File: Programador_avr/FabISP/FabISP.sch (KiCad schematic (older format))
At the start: 14 parts, among them IC1 ATTINY44-SSU, M1 Reson., M2 PINHD-1x02-SMD-HEADER, M3 MICRO-USB_1_64, M4 PINHD-1x02-SMD-HEADER

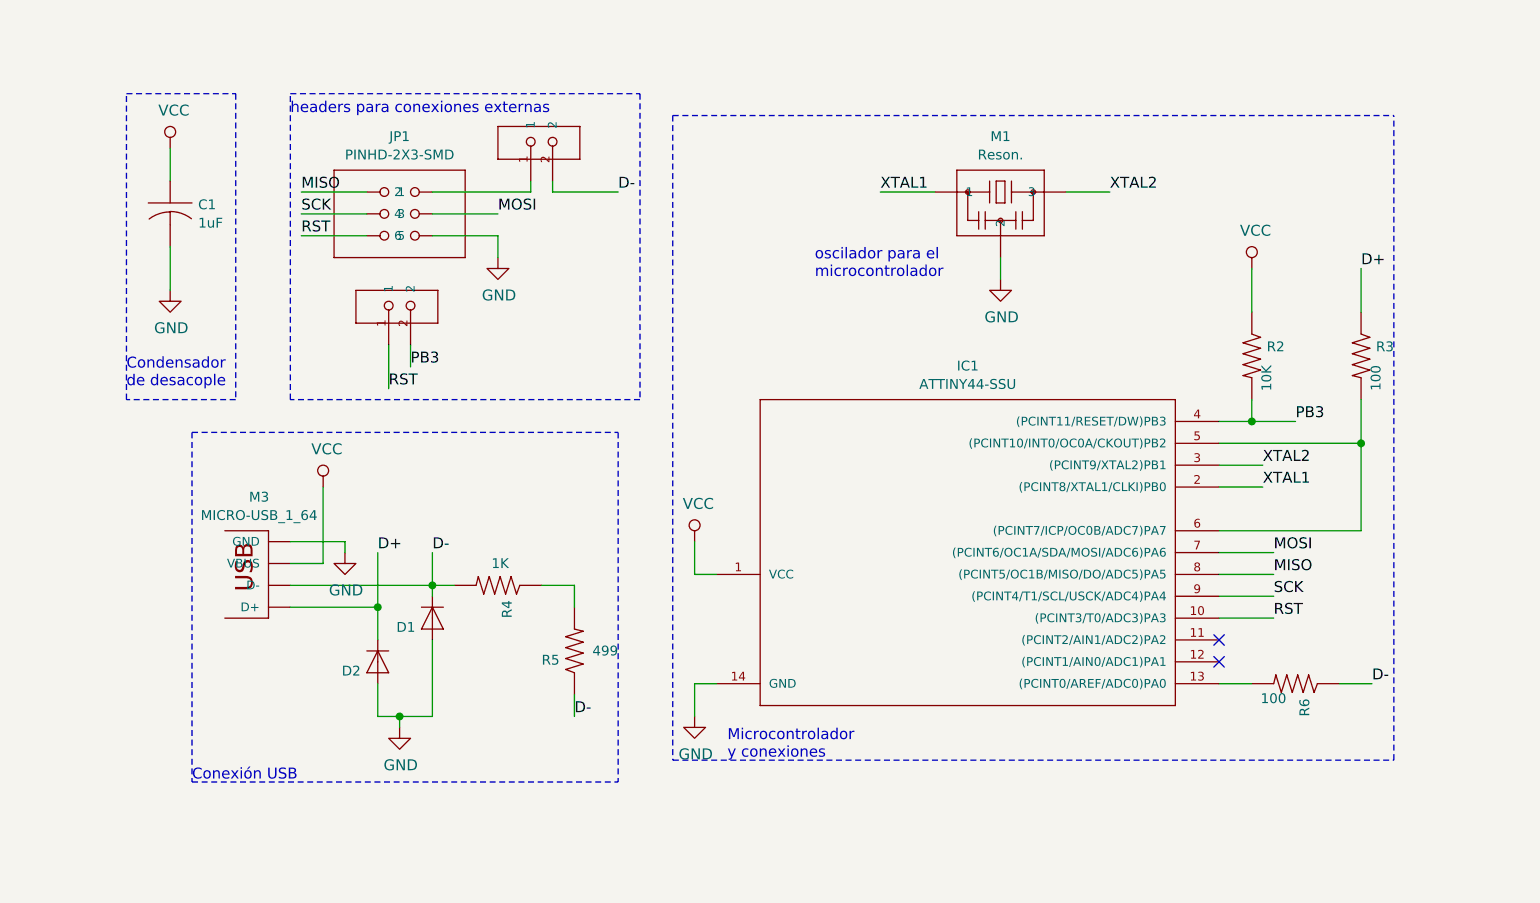
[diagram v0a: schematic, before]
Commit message: Corrección SCH Se hicieron las conexiones reemplazando etiquetas se agrego información de componentes se agregó información solicitada
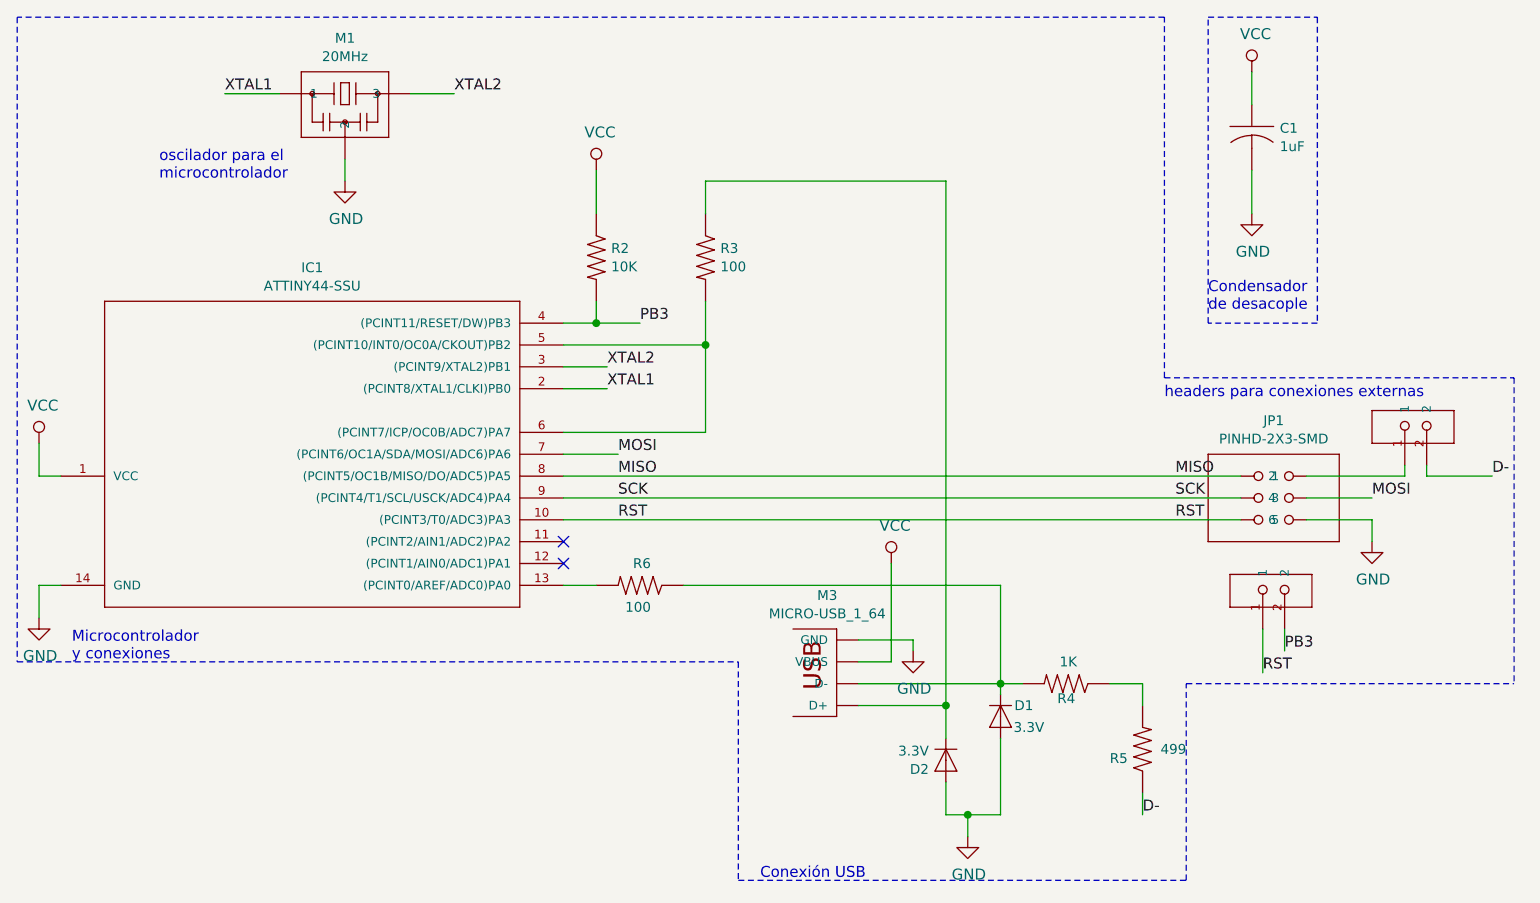
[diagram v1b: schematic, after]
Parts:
- D1, D2: value (none) -> 3.3V
- M1: value Reson. -> 20MHz
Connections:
- net D-: no longer D1.CATHODE (C), M3.D-, R4.2, R6.1
- net D+: no longer names the net of D2.CATHODE (C), M3.D+, R3.1
- new net: D1.CATHODE (C), M3.D-, R4.2, R6.1
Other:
- moved on the sheet: C1, D1, D2, IC1, JP1, M1, M3, R2, R3, R4, R5, R6

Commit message: se agrego componentes en 3D se corrigió nodo tierra y esquemático, se agregó agujero de sujeción
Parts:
- removed M4: PINHD-1x02-SMD-HEADER, Connector_PinHeader_1.00mm:PinHeader_2x01_P1.00mm_Vertical_SMD, symbol fab:PINHD-1x02-SMD-HEADER
- added H1, H2, H3: MountingHole, MountingHole:MountingHole_2.1mm, symbol Mechanical:MountingHole
- added H4: MountingHole, MountingHole:MountingHole_2.2mm_M2, symbol Mechanical:MountingHole
- added R1: 0, Resistor_SMD:R_1206_3216Metric, symbol fab:RES-US1206FAB
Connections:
- net D- is gone; now on an unnamed net: R5.1
- net VCC: now also R5.2, R1.1
- net at JP1.2: now also R1.2
- net at R4.1: no longer R5.2
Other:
- moved on the sheet: R5

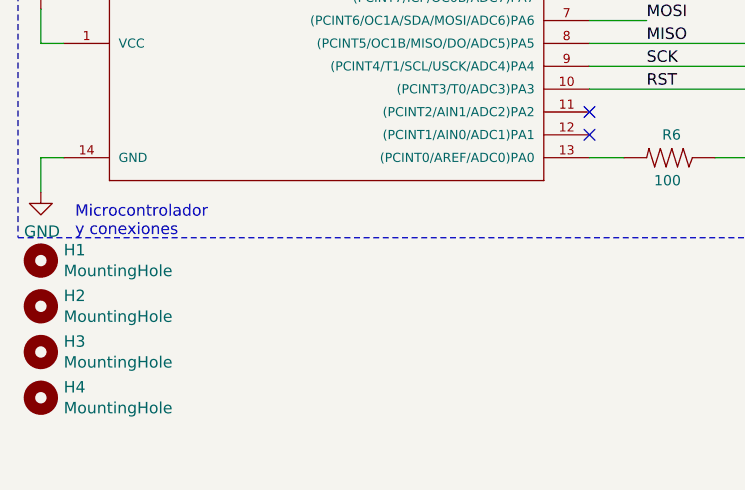
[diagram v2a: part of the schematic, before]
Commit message: fiduciales y mejora de distribución
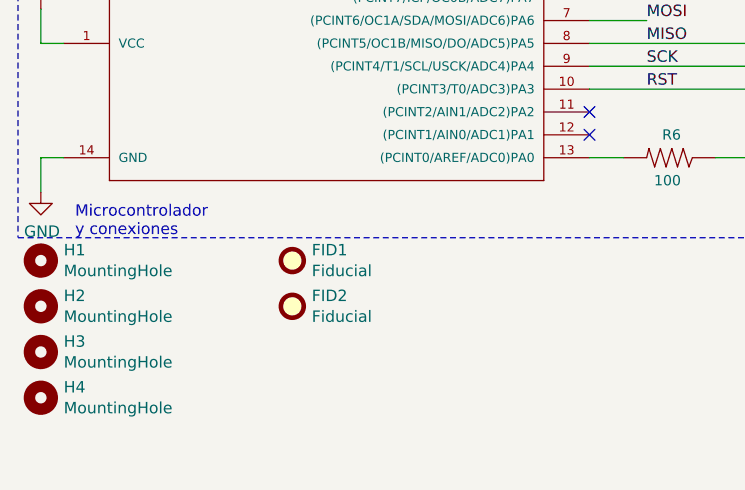
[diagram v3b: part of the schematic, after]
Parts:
- added FID1, FID2: Fiducial, Fiducial:Fiducial_1mm_Mask2mm, symbol Mechanical:Fiducial
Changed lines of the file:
@@
 Wire Wire Line
 	9250 4150 9250 4000
+$Comp
+L Mechanical:Fiducial FID1
+U 1 1 5FB56B2E
+P 3700 5100
+F 0 "FID1" H 3785 5146 50  0000 L CNN
+F 1 "Fiducial" H 3785 5055 50  0000 L CNN
+F 2 "Fiducial:Fiducial_1mm_Mask2mm" H 3700 5100 50  0001 C CNN
+F 3 "~" H 3700 5100 50  0001 C CNN
+	1    3700 5100
+	1    0    0    -1
+$EndComp
+$Comp
+L Mechanical:Fiducial FID2
+U 1 1 5FB573C0
+P 3700 5300
+F 0 "FID2" H 3785 5346 50  0000 L CNN
+F 1 "Fiducial" H 3785 5255 50  0000 L CNN
+F 2 "Fiducial:Fiducial_1mm_Mask2mm" H 3700 5300 50  0001 C CNN
+F 3 "~" H 3700 5300 50  0001 C CNN
+	1    3700 5300
+	1    0    0    -1
+$EndComp
 $EndSCHEMATC
